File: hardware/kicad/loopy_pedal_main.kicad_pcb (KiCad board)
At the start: 2 copper layers, 82 x 84 mm, 84 parts, among them J1 USB, J10 MOCO, J11 IND, J12 UNDO, J13 MODE, J14 TRACK1, J15 TRACK2, J16 TRACK3, J17 TRACK4, J18 CLEAR, J19 BANK, J2 9V, J3 RECPLAY, J4 STOP, J5 RING, J6 ICSP U1, J7 ICSP U2, J8 MIDI OUT, J9 MIDI IN, Q1 AO3401A, SW1 RST U1, SW2 RST U2, U1 ATmega328P-A, U10 74AHCT1G08, U2 ATmega16U2-A, U3 AP63203WU, U4 74AHCT1G125, U5 LM66100DCK, U6 LM66100DCK, U7 USBLC6-2SC6, U8 74AHCT1G125, U9 H11L1, Y1 16MHz, Y2 16MHz

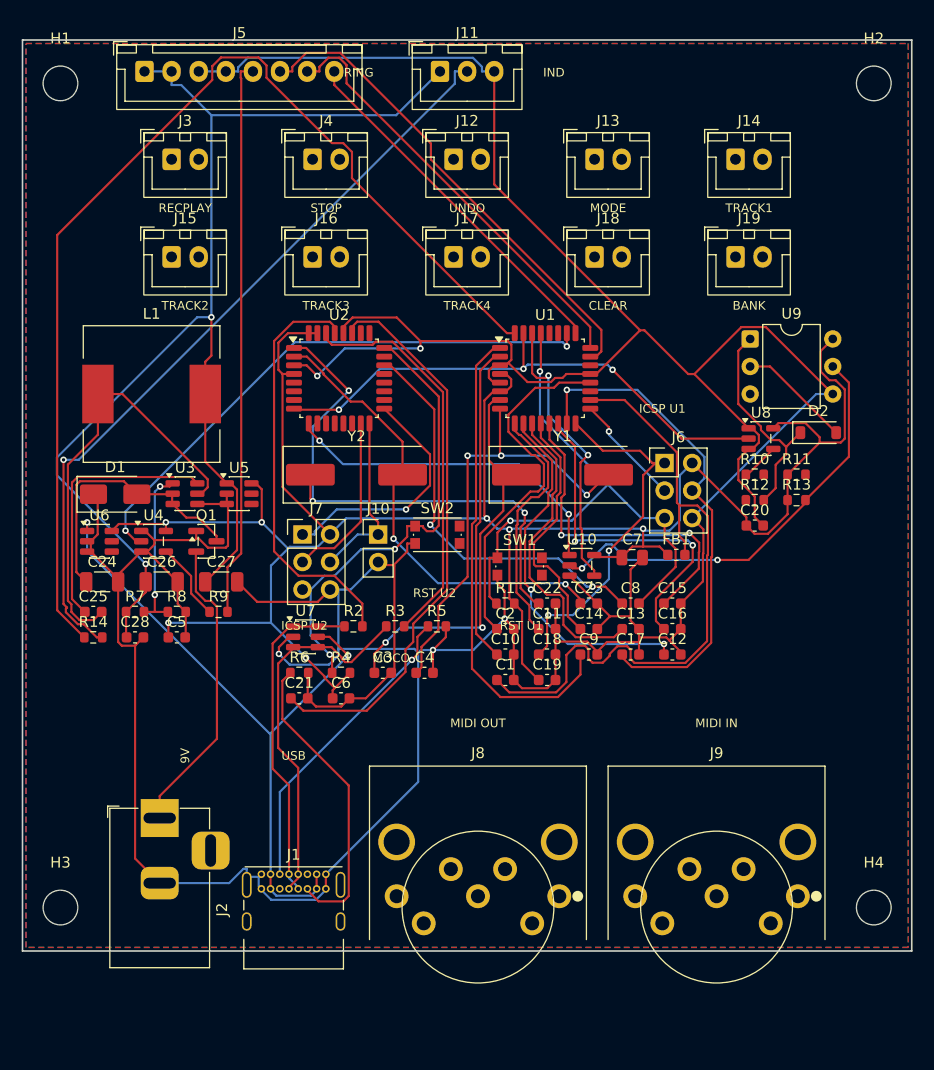
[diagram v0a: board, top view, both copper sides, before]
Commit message: fix(pcb): make every silkscreen label readable (reserved label gaps)
The dev-header labels (ICSP U1/U2, MOCO, RST U1/U2) previously overlapped the
densely-packed parts. Reserve a clear gap under each dev header in the packer
(inflate its packing height, drop the part at the top of the slot, place the
label in the gap) so every label sits in clear space. Nudge RING/IND into the
top-edge gap. Board grows 82x84 -> 82x90 to absorb the gaps; re-routed, DRC 0/0.
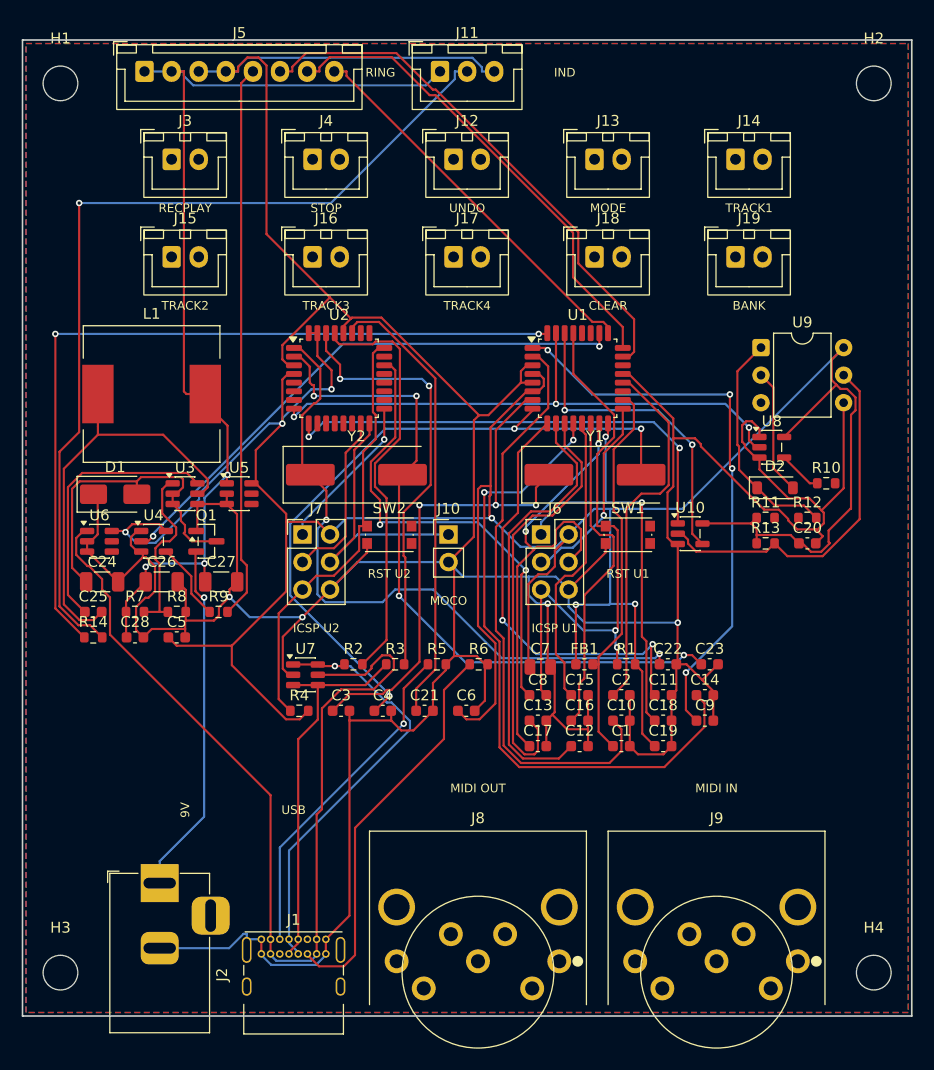
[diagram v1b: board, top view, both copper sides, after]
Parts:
- moved R6 16.6 mm to (72.1, 87.6)
- moved FB1 13.2 mm to (81.8, 87.6)
- moved C7 13.2 mm to (77.7, 87.8)
- moved J6 13.2 mm to (77.8, 75.6)
- moved C22 12.5 mm to (89.5, 87.6)
- moved C23 12.5 mm to (93.4, 87.6)
- moved R1 12.5 mm to (85.7, 87.6)
- moved C11 12.3 mm to (89.1, 90.4)
- moved C14 12.3 mm to (92.9, 90.4)
- moved C18 12.3 mm to (89.1, 92.8)
- moved C19 12.3 mm to (89.1, 95.1)
- moved C9 12.3 mm to (92.9, 92.8)
- moved C2 12.3 mm to (85.2, 90.4)
- moved C1 12.3 mm to (85.2, 95.1)
- moved C10 12.3 mm to (85.2, 92.8)
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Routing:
- net +5V: track 200.5 -> 280.6 mm, vias 7 -> 6
- net SW_TRACK2: track 23.1 -> 60.3 mm, vias 0 -> 2
- net VBUS: track 61.6 -> 91.9 mm, vias 2 -> 0
- net IND_DATA: track 100.5 -> 74.5 mm, vias 0 -> 2
- net N$1: track 61.3 -> 35.7 mm
- net SW_STOP: track 29.5 -> 54.2 mm
- net +5V_LED: track 117.6 -> 94.4 mm, vias 2 -> 3
- net N$4: track 41.7 -> 64.4 mm
- net N$8: track 42.6 -> 64.4 mm, vias 2 -> 4
- net SW_UNDO: track 22.8 -> 40.3 mm, vias 0 -> 2
- net IND_DATA_OUT: track 71.3 -> 84.3 mm
- net N$3: track 37.2 -> 49.8 mm, vias 2 -> 3
- net M16_TXD: track 31.6 -> 44.0 mm
- net N$7: track 50.1 -> 62.2 mm, vias 3 -> 2
- net SW_TRACK1: track 28.7 -> 39.8 mm
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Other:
- board size 82 x 84 mm -> 82 x 90 mm
